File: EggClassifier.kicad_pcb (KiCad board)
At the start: 2 copper layers, 140 x 80 mm, 77 parts, among them J1 ST-LINK, J10 LCD_CHAR, J11 SERVO2, J12 BME280, J13 UART1, J14 FAN, J15 UART2, J16 AS7265X, J17 TFT_SPI, J2 USB_A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

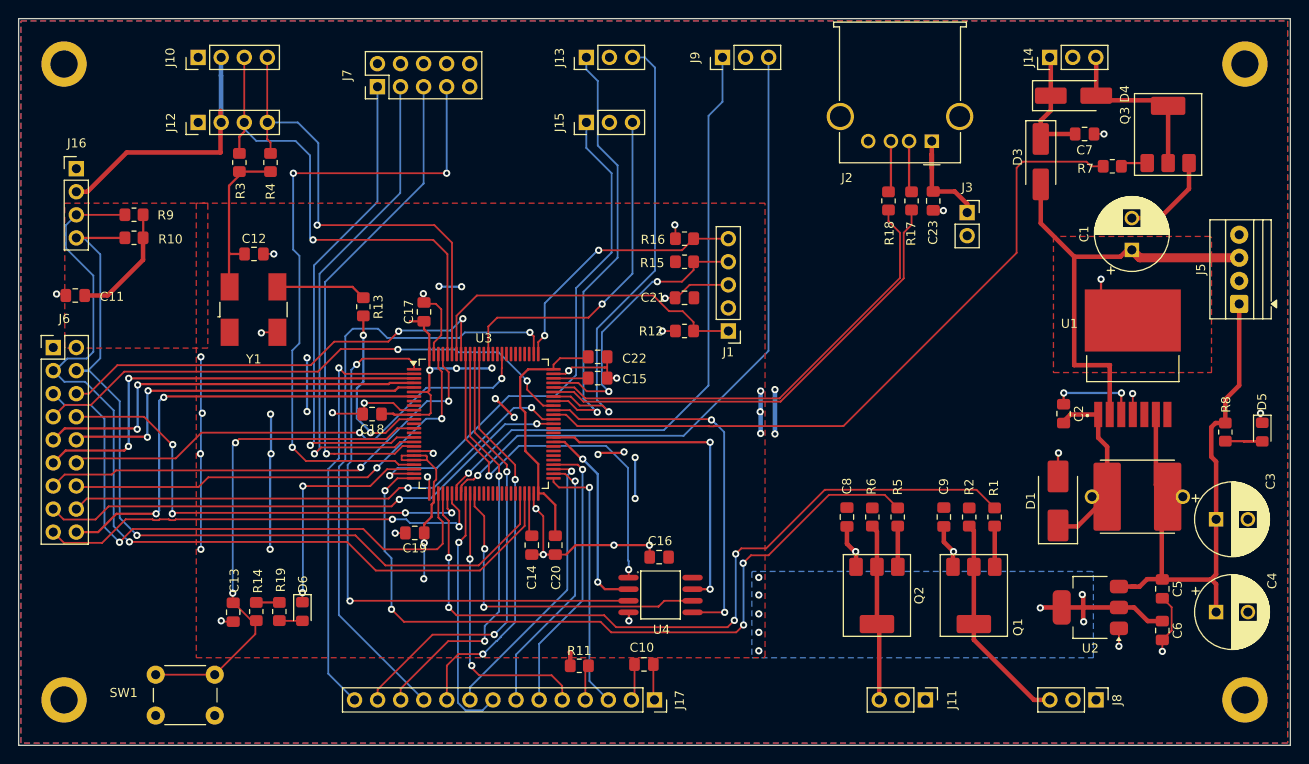
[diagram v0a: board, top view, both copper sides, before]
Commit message: finished layout;. H743 with SD-Card
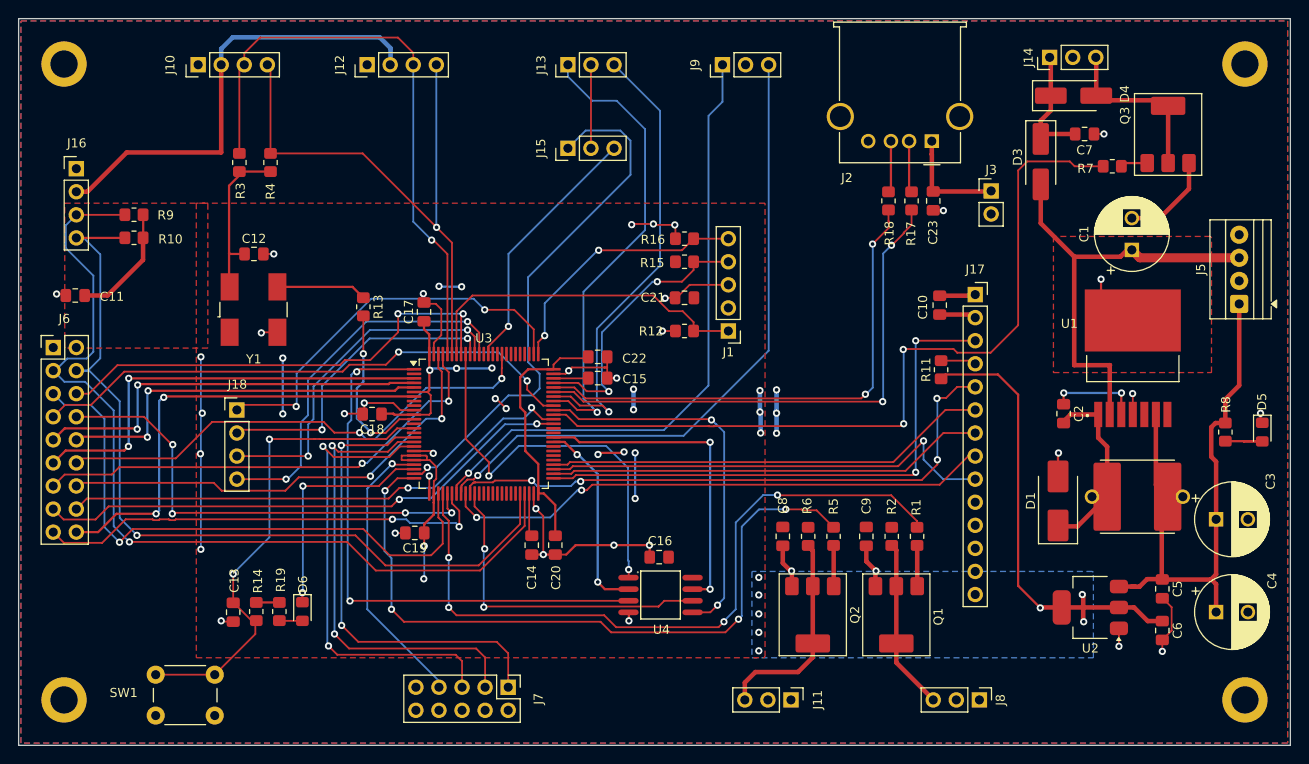
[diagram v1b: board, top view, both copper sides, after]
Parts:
- added J18: SD_CARD, EggClassifier:PinHeader_1x04_P2.54mm_Vertical, F.Cu at (104.0, 83.1)
- J3: footprint EggClassifier:PinSocket_1x02_P2.54mm_Vertical -> Connector_PinHeader_2.54mm:PinHeader_1x02_P2.54mm_Vertical
- moved J7 67.7 mm to (133.9, 113.6), turned to -90 degrees
- moved J17 56.9 mm to (185.3, 70.4), turned to 0 degrees
- moved R11 51.5 mm to (181.6, 78.7), turned to 90 degrees
- moved C10 51.2 mm to (181.4, 71.5), turned to -90 degrees
- moved J12 19.7 mm to (118.4, 45.1)
- moved J11 14.8 mm to (165.0, 115.0)
- moved J8 12.8 mm to (185.8, 115.0)
- moved C9 8.80 mm to (173.3, 97.0)
- moved Q1 8.80 mm to (176.6, 105.6)
- moved R1 8.80 mm to (178.9, 97.0)
- moved R2 8.80 mm to (176.1, 97.0)
- moved C8 7.38 mm to (164.1, 97.0)
- moved Q2 7.38 mm to (167.4, 105.6)
- moved R5 7.38 mm to (169.7, 97.0)
- moved R6 7.38 mm to (166.9, 97.0)
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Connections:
- J17 pad 10: SPI1_SCK -> unconnected-(J17-Pin_10-Pad10)
- J17 pad 11: SPI1_NCS -> unconnected-(J17-Pin_11-Pad11)
- J17 pad 12: SPI1_MOSI -> unconnected-(J17-Pin_12-Pad12)
- J17 pad 13: SPI1_MISO -> unconnected-(J17-Pin_13-Pad13)
- J17 pad 14: TFT_INT -> unconnected-(J17-Pin_14-Pad14)
- U3 pad 2: TFT_INT -> unconnected-(U3-PE3-Pad2)
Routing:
- net TFT_INT: track 46.8 -> 0.00 mm, vias 1 -> 0
- net USER_GPIO4: track 71.4 -> 30.8 mm, vias 3 -> 1
- net TFT_RS: track 31.6 -> 65.8 mm, vias 2 -> 4
- net TFT_BL: track 28.1 -> 60.8 mm, vias 1 -> 2
- net SPI2_NCS: track 28.9 -> 61.2 mm, vias 1 -> 2
- net SPI1_NCS: track 68.1 -> 44.2 mm, vias 1 -> 2
- net VCC: track 104.0 -> 125.5 mm, vias 2 -> 3
- net +3.3V: track 181.0 -> 200.4 mm, vias 29 -> 28
- net SPI2_SCK: track 29.5 -> 48.3 mm, vias 1 -> 0
- net SPI2_MISO: track 31.9 -> 50.7 mm
- net SPI2_MOSI: track 30.8 -> 48.9 mm, vias 1 -> 0
- net SPI1_MOSI: track 46.2 -> 33.9 mm
- net GND: track 122.1 -> 133.5 mm, vias 34 -> 36
- net SPI1_MISO: track 49.4 -> 38.3 mm
- net I2C1_SDA: track 55.2 -> 66.2 mm
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
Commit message: final version of 80mmx140mm PCB
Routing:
- net GND: track 133.5 -> 132.7 mm
- net Net-(U3-PH0): track 19.2 -> 18.5 mm
- net SPI1_MISO: track 38.3 -> 39.0 mm
- net SPI1_MOSI: track 33.9 -> 34.5 mm
- net SPI1_SCK: track 41.8 -> 42.3 mm

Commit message: Snapshot prior to making JLC version
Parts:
- J3: footprint Connector_PinHeader_2.54mm:PinHeader_1x02_P2.54mm_Vertical -> EggClassifier:PinHeader_1x02_P2.54mm_Vertical
- Y1: footprint EggClassifier:Oscillator_SMD_Abracon_ASV-4Pin_7.0x5.1mm_HandSoldering -> EggClassifier:Oscillator_SMD_SeikoEpson_SG8002CA-4Pin_7.0x5.0mm
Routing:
- net ADC_IN2: track 72.1 -> 71.5 mm
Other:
- board text added: "DCMI_CAMERA"

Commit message: end of day snapshot
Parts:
- J18: footprint EggClassifier:PinHeader_1x04_P2.54mm_Vertical -> EggClassifier:PinSocket_1x04_P2.54mm_Vertical
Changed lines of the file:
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@@
 		(sheetname "/BASEBOARD/")
 		(sheetfile "baseboard.kicad_sch")
-		(attr through_hole)
+		(attr through_hole exclude_from_bom)
 		(fp_line
 			(start -1.33 -1.33)
@@
 		(sheetname "/BASEBOARD/")
 		(sheetfile "baseboard.kicad_sch")
-		(attr through_hole)
+		(attr through_hole exclude_from_bom)
 		(fp_line
 			(start -1.33 6.41)
@@
 		(sheetname "/BASEBOARD/")
 		(sheetfile "baseboard.kicad_sch")
-		(attr through_hole)
+		(attr through_hole exclude_from_bom)
 		(fp_line
 			(start -1.33 -1.33)
@@
 		(sheetname "/DevEBox/")
 		(sheetfile "devebox.kicad_sch")
-		(attr through_hole)
+		(attr through_hole exclude_from_bom)
 		(fp_line
 			(start 1.33 1.27)
@@
 		(sheetname "/DevEBox/")
 		(sheetfile "devebox.kicad_sch")
-		(attr through_hole)
+		(attr through_hole exclude_from_bom)
 		(fp_line
 			(start 6.75 3)
@@
 	)
 	(footprint "EggClassifier:PinSocket_1x14_P2.54mm_Vertical"
-		(locked yes)
 		(layer "F.Cu")
 		(at 185.3084 70.3784)
@@
 		(sheetname "/BASEBOARD/")
 		(sheetfile "baseboard.kicad_sch")
-		(attr through_hole)
+		(attr through_hole exclude_from_bom)
 		(fp_line
 			(start -1.33 1.27)
@@
 		(tags "SMD SMT crystal oscillator")
 		(property "Reference" "Y1"
-			(at 5.3086 0.4064 0)
+			(at 0 -4.1 0)
 			(layer "F.SilkS")
 			(effects
@@
 		(attr smd)
 		(fp_line
+			(start -3.7 -2.7)
+			(end -3.64 -2.7)
+			(stroke
+				(width 0.12)
+				(type solid)
+			)
+			(layer "F.SilkS")
+		)
+		(fp_line
 			(start -3.7 2.7)
 			(end -3.7 -2.7)
@@
 		)
 		(fp_line
-			(start -1.3 -2.7)
-			(end 1.3 -2.7)
+			(start -3.64 2.7)
+			(end -3.7 2.7)
 			(stroke
 				(width 0.12)
@@
 		)
 		(fp_line
-			(start -1.3 2.7)
-			(end -1.3 3.3)
+			(start -3.64 3.3)
+			(end -3.64 2.7)
 			(stroke
 				(width 0.12)
@@
 		)
 		(fp_line
-			(start 1.3 2.7)
-			(end -1.3 2.7)
+			(start -1.44 -2.7)
+			(end 1.44 -2.7)
+			(stroke
+				(width 0.12)
+				(type solid)
+			)
+			(layer "F.SilkS")
+		)
+		(fp_line
+			(start -1.44 2.7)
+			(end -1.44 3.3)
+			(stroke
+				(width 0.12)
+				(type solid)
+			)
+			(layer "F.SilkS")
+		)
+		(fp_line
+			(start 1.44 2.7)
+			(end -1.44 2.7)
+			(stroke
+				(width 0.12)
+				(type solid)
+			)
+			(layer "F.SilkS")
+		)
+		(fp_line
+			(start 3.64 -2.7)
+			(end 3.7 -2.7)
 			(stroke
 				(width 0.12)
@@
 			(layer "F.SilkS")
 		)
+		(fp_line
+			(start 3.7 2.7)
+			(end 3.64 2.7)
+			(stroke
+				(width 0.12)
+				(type solid)
+			)
+			(layer "F.SilkS")
+		)
 		(fp_circle
 			(center 0 0)
@@
 		(sheetname "/BASEBOARD/")
 		(sheetfile "baseboard.kicad_sch")
-		(attr through_hole)
+		(attr through_hole exclude_from_bom)
 		(fp_line
 			(start -1.33 -1.33)
@@
 	)
 	(footprint "EggClassifier:R_0805_2012Metric_Pad1.20x1.40mm_HandSolder"
-		(locked yes)
 		(layer "F.Cu")
 		(at 181.551 78.6524 90)
@@
 		(sheetname "/BASEBOARD/")
 		(sheetfile "baseboard.kicad_sch")
-		(attr through_hole)
+		(attr through_hole exclude_from_bom)
 		(fp_line
 			(start -1.33 -1.33)
@@
 		(sheetname "/BASEBOARD/")
 		(sheetfile "baseboard.kicad_sch")
-		(attr through_hole)
+		(attr through_hole exclude_from_bom)
 		(fp_line
 			(start -1.33 -1.33)
@@
 		(sheetname "/BASEBOARD/")
 		(sheetfile "baseboard.kicad_sch")
-		(attr through_hole)
+		(attr through_hole exclude_from_bom)
 		(fp_line
 			(start -1.33 -1.33)
@@
 		(sheetname "/BASEBOARD/")
 		(sheetfile "baseboard.kicad_sch")
-		(attr through_hole)
+		(attr through_hole exclude_from_bom)
 		(fp_line
 			(start -1.33 -1.33)
@@
 		(sheetname "/DevEBox/")
 		(sheetfile "devebox.kicad_sch")
-		(attr through_hole)
+		(attr through_hole exclude_from_bom)
 		(fp_line
 			(start 10.81 13.1)
@@
 	)
 	(footprint "EggClassifier:C_0805_2012Metric_Pad1.18x1.45mm_HandSolder"
-		(locked yes)
 		(layer "F.Cu")
 		(at 181.3986 71.5404 -90)
@@
 		(sheetname "/BASEBOARD/")
 		(sheetfile "baseboard.kicad_sch")
-		(attr through_hole)
+		(attr through_hole exclude_from_bom)
 		(fp_line
 			(start -1.33 11.49)
@@
 		(sheetname "/BASEBOARD/")
 		(sheetfile "baseboard.kicad_sch")
-		(attr through_hole)
+		(attr through_hole exclude_from_bom)
 		(fp_line
 			(start 9.26 -3.22)
@@
 		)
 	)
-	(footprint "EggClassifier:PinHeader_1x04_P2.54mm_Vertical"
-		(locked yes)
+	(footprint "EggClassifier:PinSocket_1x04_P2.54mm_Vertical"
 		(layer "F.Cu")
 		(at 104.0284 83.0784)
-		(descr "Through hole straight pin header, 1x04, 2.54mm pitch, single row")
-		(tags "Through hole pin header THT 1x04 2.54mm single row")
+		(descr "Through hole straight socket strip, 1x04, 2.54mm pitch, single row (from Kicad 4.0.7), script generated")
+		(tags "Through hole socket strip THT 1x04 2.54mm single row")
 		(property "Reference" "J18"
-			(at 0.0508 -2.804 0)
+			(at 0 -2.77 0)
 			(layer "F.SilkS")
 			(effects
@@
 		)
 		(property "Value" "SD_CARD"
-			(at 0 9.95 0)
+			(at 0 10.39 0)
 			(layer "F.Fab")
 			(effects
@@
 		(sheetname "/BASEBOARD/")
 		(sheetfile "baseboard.kicad_sch")
-		(attr through_hole)
+		(attr through_hole exclude_from_bom)
 		(fp_line
-			(start -1.33 -1.33)
-			(end 0 -1.33)
+			(start -1.33 1.27)
+			(end -1.33 8.95)
 			(stroke
 				(width 0.12)
@@
 		)
 		(fp_line
-			(start -1.33 0)
-			(end -1.33 -1.33)
+			(start -1.33 1.27)
+			(end 1.33 1.27)
 			(stroke
 				(width 0.12)
@@
 		)
 		(fp_line
-			(start -1.33 1.27)
-			(end -1.33 8.95)
+			(start -1.33 8.95)
+			(end 1.33 8.95)
 			(stroke
 				(width 0.12)
@@
 		)
 		(fp_line
-			(start -1.33 1.27)
-			(end 1.33 1.27)
+			(start 0 -1.33)
+			(end 1.33 -1.33)
 			(stroke
 				(width 0.12)
@@
 		)
 		(fp_line
-			(start -1.33 8.95)
-			(end 1.33 8.95)
+			(start 1.33 -1.33)
+			(end 1.33 0)
 			(stroke
 				(width 0.12)
@@
 		(fp_line
 			(start -1.8 -1.8)
-			(end -1.8 9.4)
+			(end 1.75 -1.8)
 			(stroke
 				(width 0.05)
@@
 		(fp_line
 			(start -1.8 9.4)
-			(end 1.8 9.4)
+			(end -1.8 -1.8)
 			(stroke
 				(width 0.05)
@@
 		)
 		(fp_line
-			(start 1.8 -1.8)
-			(end -1.8 -1.8)
+			(start 1.75 -1.8)
+			(end 1.75 9.4)
 			(stroke
 				(width 0.05)
@@
 		)
 		(fp_line
-			(start 1.8 9.4)
-			(end 1.8 -1.8)
+			(start 1.75 9.4)
+			(end -1.8 9.4)
 			(stroke
 				(width 0.05)
@@
 		)
 		(fp_line
-			(start -1.27 -0.635)
-			(end -0.635 -1.27)
+			(start -1.27 -1.27)
+			(end 0.635 -1.27)
 			(stroke
 				(width 0.1)
@@
 		(fp_line
 			(start -1.27 8.89)
-			(end -1.27 -0.635)
+			(end -1.27 -1.27)
 			(stroke
 				(width 0.1)
@@
 		)
 		(fp_line
-			(start -0.635 -1.27)
-			(end 1.27 -1.27)
+			(start 0.635 -1.27)
+			(end 1.27 -0.635)
 			(stroke
 				(width 0.1)
@@
 		)
 		(fp_line
-			(start 1.27 -1.27)
+			(start 1.27 -0.635)
 			(end 1.27 8.89)
 			(stroke
@@
 		)
 		(embedded_fonts no)
-		(model "${KICAD9_3DMODEL_DIR}/Connector_PinHeader_2.54mm.3dshapes/PinHeader_1x04_P2.54mm_Vertical.wrl"
+		(model "${KICAD9_3DMODEL_DIR}/Connector_PinSocket_2.54mm.3dshapes/PinSocket_1x04_P2.54mm_Vertical.wrl"
 			(offset
 				(xyz 0 0 0)
@@
 		(sheetname "/BASEBOARD/")
 		(sheetfile "baseboard.kicad_sch")
-		(attr through_hole)
+		(attr through_hole exclude_from_bom)
 		(fp_line
 			(start -1.33 6.41)
@@
 		(sheetname "/BASEBOARD/")
 		(sheetfile "baseboard.kicad_sch")
-		(attr through_hole)
+		(attr through_hole exclude_from_bom)
 		(fp_line
 			(start -1.33 -1.33)
@@
 		(sheetname "/BASEBOARD/")
 		(sheetfile "baseboard.kicad_sch")
-		(attr through_hole)
+		(attr through_hole exclude_from_bom)
 		(fp_line
 			(start -1.33 -1.33)
@@
 	)
 	(group ""
-		(locked yes)
 		(members "49ca7413-1c70-41ee-96a4-ed4b19193ca4" "5ac1bfb4-5686-4b70-8e50-649a0d05032b"
 			"aa5dcacd-b810-4084-ac85-26a0f9913147" "cdb487e0-ba58-40d5-9924-35f158fe1b2a"
